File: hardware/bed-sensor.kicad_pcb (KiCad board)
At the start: 2 copper layers, 21.3 x 43.2 mm, 46 parts, among them J1 USB_B_Mini, J2 Conn_ARM_JTAG_SWD_10, J3 DM3AT-SF-PEJM5, J4 Conn_01x02, Q1 Q_PMOS_GSD, SW1 SW_Push, U1 MCP73831-2-OT, U2 TLV70218_SOT23-5, U3 AP2112K-3.3, U4 MDBT50Q-1M, U5 PCA9306, U6 ICM-20948, U7 BMP280, Y1 32.768

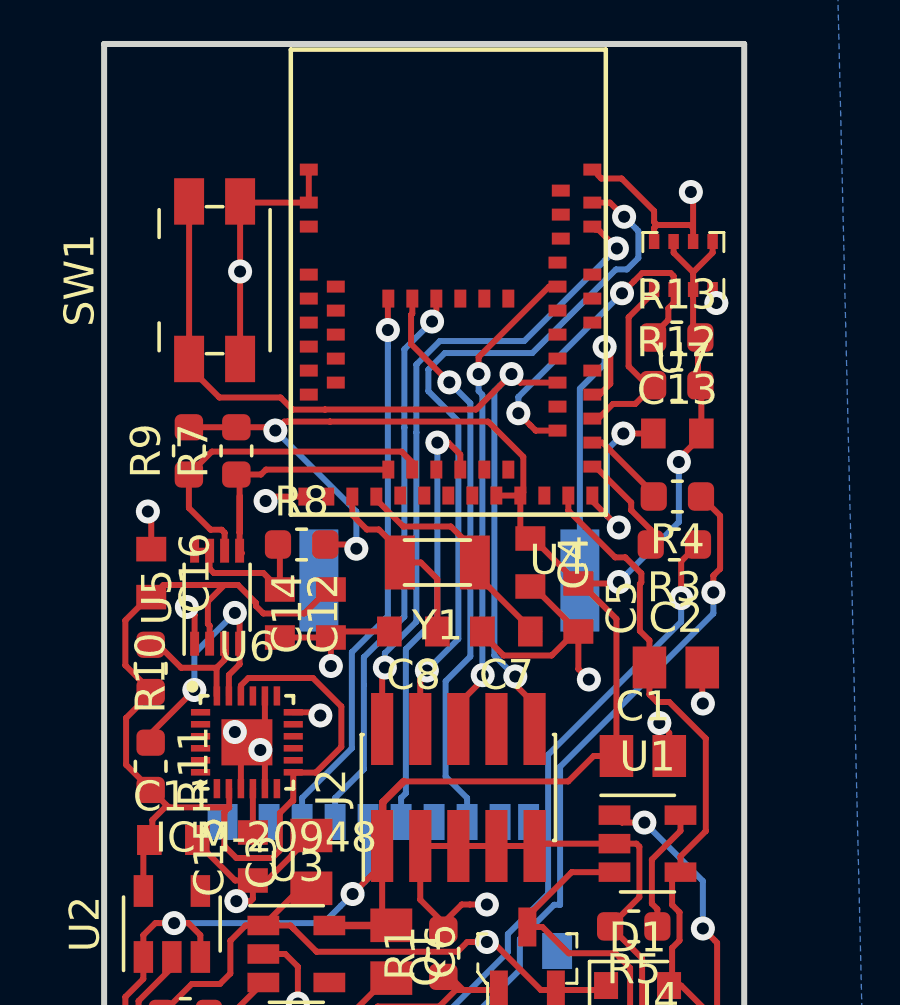
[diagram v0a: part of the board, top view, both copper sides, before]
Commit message: updated and added csv
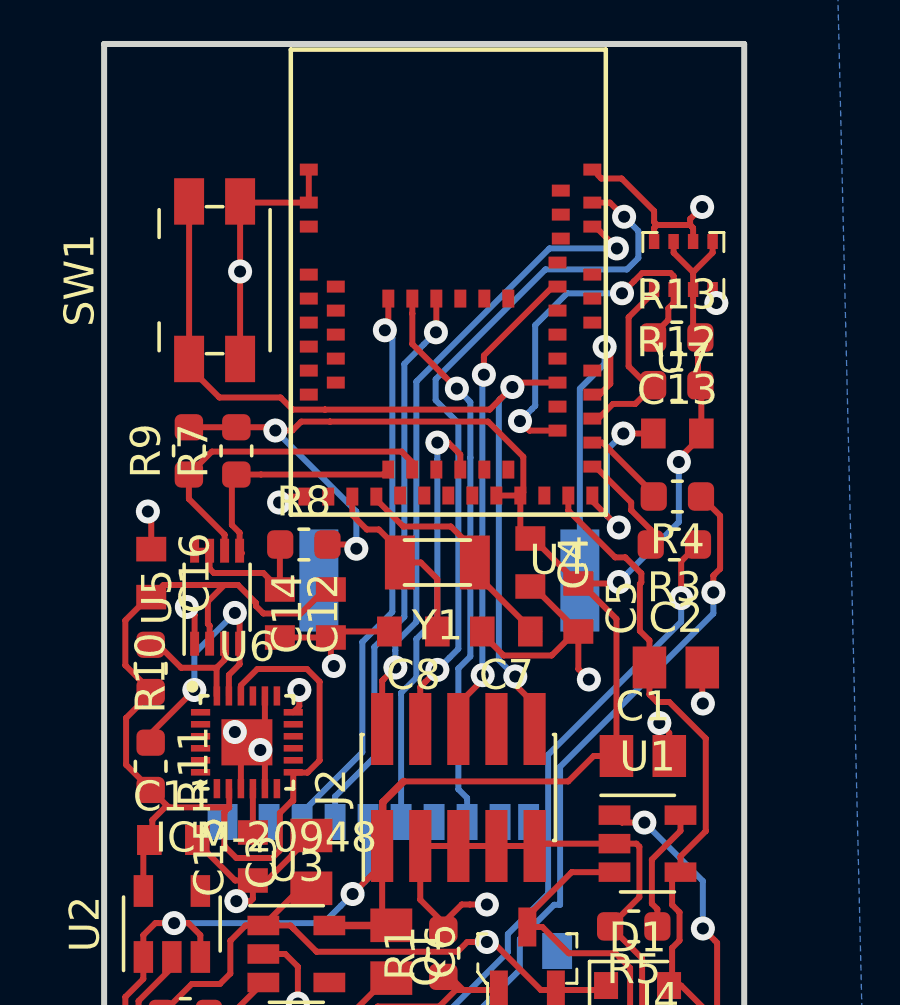
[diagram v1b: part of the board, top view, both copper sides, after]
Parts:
- moved R8 0.08 mm to (120.5, -33.1)
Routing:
- net BMP_SDA: track 11.7 -> 12.9 mm
- net SCL_MPU: track 9.06 -> 7.96 mm
- net GND: track 106.8 -> 105.9 mm
- net RESET: track 31.8 -> 31.1 mm
- net SWCLK: track 24.6 -> 24.1 mm

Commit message: tweaked board
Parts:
- moved BZ1 138.0 mm to (148.1, 104.2)
- moved C1 138.0 mm to (154.5, 110.1)
- moved C10 138.0 mm to (139.6, 121.8)
- moved C11 138.0 mm to (138.9, 112.9)
- moved C12 138.0 mm to (142.4, 105.3)
- moved C14 138.0 mm to (144.1, 105.3)
- moved C15 138.0 mm to (141.5, 113.5)
- moved C16 138.0 mm to (138.1, 104.0)
- moved C2 138.0 mm to (155.6, 107.2)
- moved C3 138.0 mm to (143.5, 113.6)
- moved C4 138.0 mm to (150.8, 103.7)
- moved C5 138.0 mm to (152.4, 105.2)
- moved C6 138.0 mm to (146.1, 116.6)
- moved C7 138.0 mm to (150.0, 106.0)
- moved C8 138.0 mm to (146.9, 106.0)
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
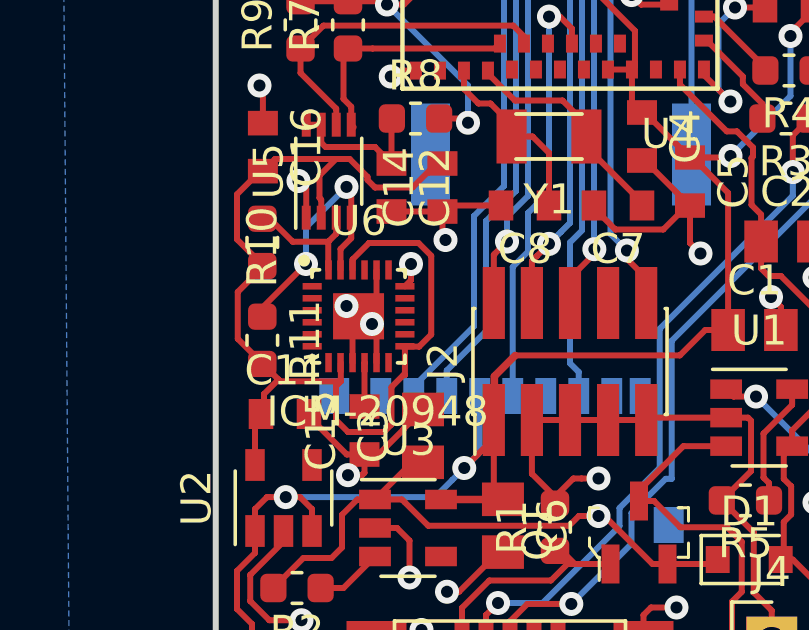
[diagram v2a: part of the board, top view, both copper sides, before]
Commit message: updated kicad and vagrant file
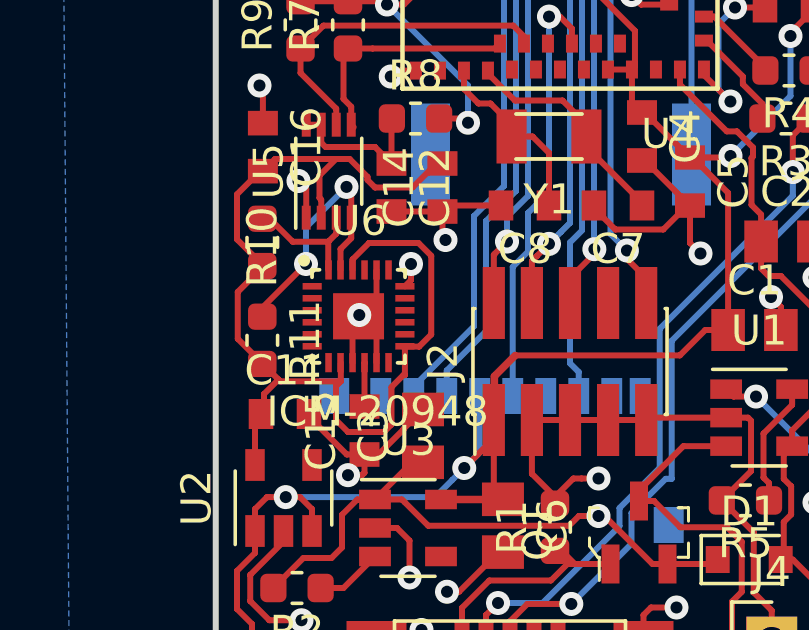
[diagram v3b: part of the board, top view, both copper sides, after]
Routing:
- net GND: vias 23 -> 22

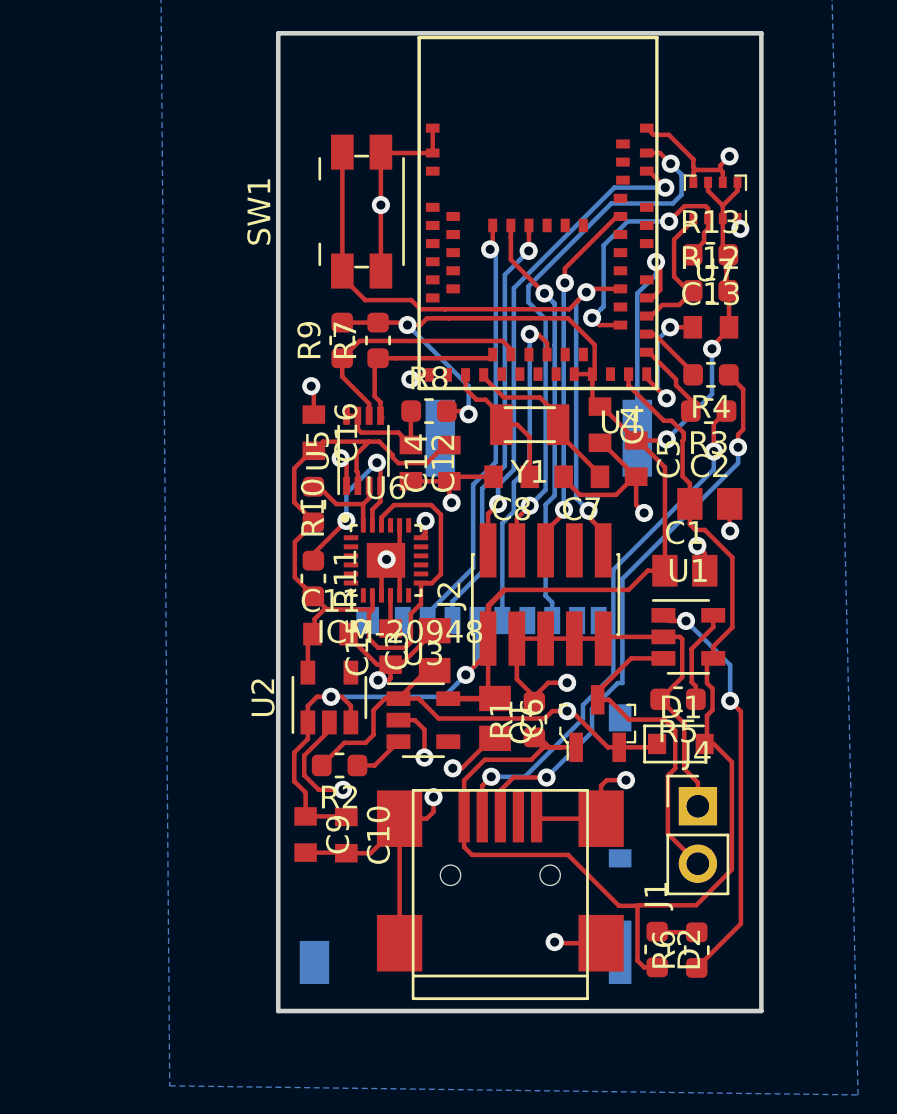
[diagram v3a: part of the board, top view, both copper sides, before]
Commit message: updated footprints
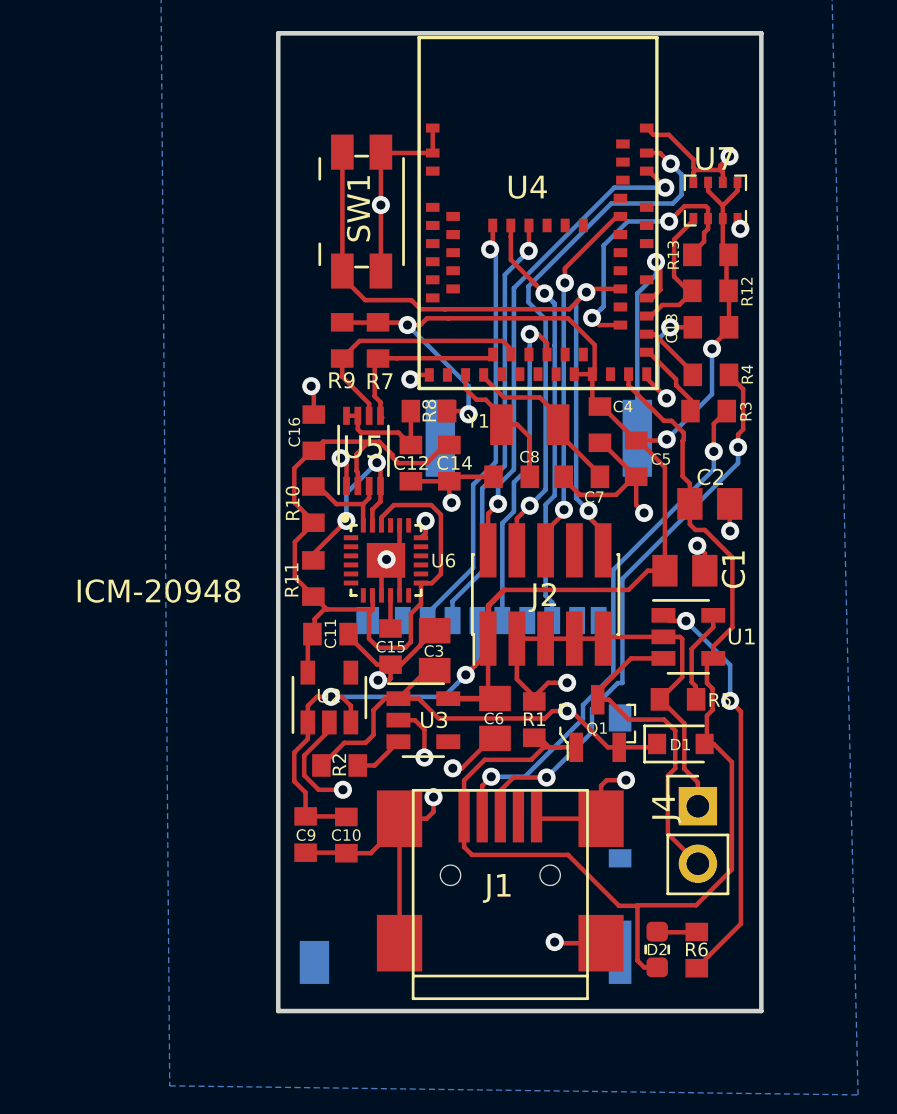
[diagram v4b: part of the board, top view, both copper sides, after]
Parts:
- R1, R10, R11, R12, R13, R2, R3, R4, R5, R6, R7, R8, R9: footprint Fuse:Fuse_0603_1608Metric -> Resistor_SMD:R_0603_1608Metric
- Y1: footprint OPL_Crystal_Oscillator:X2-SMD-3.2X1.5X0.55MM -> extra:FC-135 32.7680KA-AC3
- turned Y1 to 0 degrees

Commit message: finalized order list
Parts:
- added D3: LED_RCGB, LED_SMD:LED_Kingbright_AAA3528ESGCT, F.Cu at (138.6, 98.6)
- added R14: 330, Resistor_SMD:R_0603_1608Metric, F.Cu at (141.2, 95.5)
- added R15: 330, Resistor_SMD:R_0603_1608Metric, F.Cu at (141.1, 97.8)
- added R16: 330, Resistor_SMD:R_0603_1608Metric, F.Cu at (138.2, 95.5)
- added R17: 100k, Resistor_SMD:R_0603_1608Metric, F.Cu at (150.8, 103.8)
- added R18: 100k, Resistor_SMD:R_0603_1608Metric, F.Cu at (155.5, 105.0)
- D1: footprint Diodes_SMD:D_0805 -> Diode_SMD:D_SOD-123
- D2: footprint Capacitor_SMD:C_0603_1608Metric -> Diode_SMD:D_0603_1608Metric
- J1: footprint Connectors:USB_Mini-B -> digikey-footprints:USB_Micro_B_Female_10118194-0001LF
- moved C4 5.52 mm to (155.5, 106.5), turned to 0 degrees
- moved BZ1 3.91 mm to (147.8, 100.3)
- moved SW1 3.73 mm to (138.6, 90.9)
- moved R9 1.92 mm to (138.8, 101.8), turned to 180 degrees
- moved C2 1.15 mm to (155.8, 108.3)
- moved R7 0.99 mm to (141.1, 100.9)
- moved C1 0.51 mm to (154.0, 110.2)
- moved R4 0.49 mm to (156.1, 101.2)
- moved R13 0.42 mm to (156.0, 95.8)
- moved R12 0.42 mm to (156.0, 97.4)
- moved C13 0.42 mm to (156.0, 99.0)
- moved D1 0.38 mm to (154.7, 117.9)
- moved R3 0.35 mm to (155.6, 102.7)
- moved J1 0.06 mm to (146.3, 123.7), turned to 0 degrees
- moved U4 0.05 mm to (142.8, 102.0)
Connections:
- J1 pad 4: Net-(J1-Pad4) -> (no net)
- J2 pad 8: Net-(J2-Pad8) -> (no net)
- J3 pad 1: Net-(J3-Pad1) -> (no net)
- J3 pad 8: Net-(J3-Pad8) -> (no net)
- J3 pad SWA: Net-(J3-PadSWA) -> (no net)
- J3 pad SWB: Net-(J3-PadSWB) -> (no net)
- U2 pad 4: Net-(U2-Pad4) -> (no net)
- U3 pad 4: Net-(U3-Pad4) -> (no net)
- U4 pad 10: Net-(U4-Pad10) -> (no net)
- U4 pad 11: Net-(U4-Pad11) -> (no net)
- U4 pad 12: Net-(U4-Pad12) -> (no net)
- U4 pad 13: Net-(U4-Pad13) -> (no net)
- U4 pad 14: Net-(U4-Pad14) -> (no net)
- U4 pad 16: Net-(U4-Pad16) -> (no net)
- U4 pad 20: Net-(U4-Pad20) -> VDIV
- U4 pad 22: Net-(U4-Pad22) -> (no net)
- U4 pad 23: Net-(U4-Pad23) -> (no net)
- U4 pad 24: Net-(U4-Pad24) -> (no net)
- U4 pad 26: Net-(U4-Pad26) -> (no net)
- U4 pad 27: Net-(U4-Pad27) -> (no net)
- U4 pad 29: Net-(U4-Pad29) -> (no net)
- U4 pad 3: Net-(U4-Pad3) -> (no net)
- U4 pad 31: Net-(U4-Pad31) -> (no net)
- U4 pad 36: BMP_SDA -> (no net)
- U4 pad 38: Net-(U4-Pad38) -> SD_MISO
- U4 pad 4: Net-(U4-Pad4) -> B_LED
- U4 pad 41: Net-(U4-Pad41) -> (no net)
- U4 pad 42: Net-(U4-Pad42) -> (no net)
- U4 pad 43: Net-(U4-Pad43) -> SD_MOSI
- U4 pad 44: Net-(U4-Pad44) -> BMP_SDA
- U4 pad 45: Net-(U4-Pad45) -> (no net)
- U4 pad 46: Net-(U4-Pad46) -> (no net)
- U4 pad 48: Net-(U4-Pad48) -> (no net)
- U4 pad 5: Net-(U4-Pad5) -> (no net)
- U4 pad 50: Net-(U4-Pad50) -> (no net)
- U4 pad 52: Net-(U4-Pad52) -> (no net)
- U4 pad 54: Net-(U4-Pad54) -> (no net)
- U4 pad 57: SD_MISO -> (no net)
- U4 pad 58: SD_MOSI -> (no net)
- U4 pad 59: Net-(U4-Pad59) -> (no net)
- U4 pad 6: Net-(U4-Pad6) -> R_LED
- U4 pad 60: Net-(U4-Pad60) -> (no net)
- U4 pad 61: Net-(U4-Pad61) -> (no net)
- U4 pad 7: Net-(U4-Pad7) -> (no net)
- U4 pad 8: Net-(U4-Pad8) -> G_LED
- U4 pad 9: Net-(U4-Pad9) -> (no net)
- U6 pad 12: Net-(U6-Pad12) -> (no net)
- U6 pad 19: Net-(U6-Pad19) -> (no net)
- U6 pad 21: Net-(U6-Pad21) -> (no net)
- U6 pad 7: Net-(U6-Pad7) -> (no net)
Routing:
- net +BATT: track 14.6 -> 29.4 mm, vias 0 -> 2
- net VDIV: track 0.00 -> 10.3 mm
- net BMP_SDA: track 12.9 -> 6.33 mm, vias 2 -> 0
- net GND: track 105.9 -> 100.3 mm
- net BUZZER: track 10.2 -> 5.12 mm
- net B_LED: track 0.00 -> 5.06 mm
- net +3V3: track 83.0 -> 87.7 mm, vias 6 -> 7
- net Net-(D3-Pad3): track 0.00 -> 4.63 mm
- net USB_D+: track 25.2 -> 29.2 mm
- net RESET: track 31.1 -> 34.8 mm
- net USB_D-: track 23.2 -> 26.2 mm
- net G_LED: track 0.00 -> 2.91 mm
- net SD_CS: track 18.8 -> 21.1 mm
- net SD_MISO: track 18.5 -> 16.3 mm
- net VBUS: track 51.9 -> 54.1 mm
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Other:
- board size 21.3 x 43.2 mm -> 21.9 x 43.2 mm

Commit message: update layout
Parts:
- removed R14, R15, R16: 330, Resistor_SMD:R_0603_1608Metric
- D3: value LED_RCGB -> WS2812B; footprint LED_SMD:LED_Kingbright_AAA3528ESGCT -> LED_SMD:LED_WS2812B_PLCC4_5.0x5.0mm_P3.2mm
- SW1: moved to B.Cu
- moved SW1 6.06 mm to (138.6, 97.0), turned to 270 degrees
- moved D3 3.00 mm to (139.7, 95.8)
- moved U3 0.70 mm to (143.0, 117.4)
- moved Q1 0.60 mm to (150.7, 117.5)
- moved R1 0.60 mm to (147.9, 117.3)
- moved C6 0.60 mm to (146.1, 117.2)
- moved J4 0.50 mm to (155.1, 121.0)
- moved D1 0.45 mm to (155.2, 117.9)
- moved R17 0.15 mm to (150.8, 103.7)
- moved R6 0.10 mm to (155.0, 127.0)
- moved D2 0.10 mm to (153.3, 126.9)
- moved R8 0.09 mm to (143.3, 103.0)
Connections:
- D3 pad 1: Net-(D3-Pad1) -> +3V3
- D3 pad 2: GND -> (no net)
- D3 pad 3: Net-(D3-Pad3) -> GND
- D3 pad 4: Net-(D3-Pad4) -> NEO_LED
- U4 pad 4: B_LED -> (no net)
- U4 pad 6: R_LED -> (no net)
- U4 pad 8: G_LED -> NEO_LED
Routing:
- net +3V3: track 87.7 -> 96.0 mm
- net B_LED: track 5.06 -> 0.00 mm
- net Net-(D3-Pad3): track 4.63 -> 0.00 mm
- net NEO_LED: track 0.00 -> 3.84 mm
- net Net-(C3-Pad1): track 20.4 -> 23.4 mm
- net G_LED: track 2.91 -> 0.00 mm
- net Net-(D3-Pad1): track 2.12 -> 0.00 mm
- net VBUS: track 54.1 -> 52.1 mm
- net GND: track 100.3 -> 98.4 mm, vias 22 -> 20
- net Net-(D3-Pad4): track 1.87 -> 0.00 mm
- net R_LED: track 1.68 -> 0.00 mm
- net +BATT: track 29.4 -> 30.6 mm
- net USB_D-: track 26.2 -> 25.2 mm
- net USB_D+: track 29.2 -> 28.3 mm
- net RESET: track 34.8 -> 35.4 mm, vias 2 -> 3
